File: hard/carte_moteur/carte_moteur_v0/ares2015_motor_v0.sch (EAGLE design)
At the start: 49 parts, among them IC1 ISO7220A, Q1 AOD417, U1 DRV8828PWP, U2 PCA9685

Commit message: schematic de la carte moteur finit !
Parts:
- removed A2, A3, A4: (no value), jumper:SJ
- removed HEADER: (no value), con-lsta:FE06-1
- removed IC2: (no value), SparkFun-PowerIC:V_REG_LM1117SOT223
- removed INPUT: MMATCH-6-, jt-con-micromatch:MMATCH-6-
- removed TP1, TP2, TP3: (no value), microbuilder:TESTPOINTROUND2MM
- removed U1: DRV8828PWP, Texas Instruments_By_element14_Batch_1:DRV8828PWP
- added 3V3LDO: (no value), SparkFun-PowerIC:V_REG_LM1117SOT223
- added C10, C15, C18: 0.47uF, adafruit:C-USC0805K
- added C12, C16, C6: 0.01uF, adafruit:C-USC0805K
- added C13, C17, C9: 0.1uF, adafruit:C-USC0805K
- added LED3, LED4, LED5: rouge, adafruit:LEDCHIPLED_0805
- added MOTOR0, MOTOR1, MOTOR2, MOTOR3: DRV8828PWP, Texas Instruments_By_element14_Batch_1:DRV8828PWP
- added OUT_MOT0, OUT_MOT2, OUT_MOT3: SL-3.5-2-90G, WEIDMULLER:SL-3.5-2-90G
- added PWM_ACCES, PWM_ACCES1: MMATCH-6-, jt-con-micromatch:MMATCH-6-
- added R15, R7: 0.25, adafruit:R-US_R0805
- added R8: 330, adafruit:R-US_R0805
- added U$6: LMD128D818, ADS128D818:LMD128D818
- R3, R6: value 10k -> 330
- R5: value 10k -> 0.25
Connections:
- net VIN renamed VIN_ARDUINO
- removed net C_DIR1: HEADER.4, INPUT.5
- removed net C_DIR2: HEADER.2, INPUT.7
- removed net C_PWM1: HEADER.3, INPUT.6
- removed net C_PWM2: HEADER.1, INPUT.8
- new net ADC0: MOTOR0.ISEN, MOTOR0.ISEN_2, R10.1, U$6.IN0
- new net ADC1: MOTOR1.ISEN, MOTOR1.ISEN_2, R5.1, U$6.IN1
- new net ADC2: MOTOR2.ISEN, MOTOR2.ISEN_2, R7.1, U$6.IN2
- new net ADC3: MOTOR3.ISEN, MOTOR3.ISEN_2, R15.1, U$6.IN3
- new net ADC4: U$6.IN4
- new net ADC5: U$6.IN5
- new net ADC6: U$6.IN6
- new net ADC7: U$6.IN7
- new net N$16: MOTOR0.OUT1, MOTOR0.OUT1_2, OUT_MOT0.1
- new net N$33: MOTOR1.OUT1, MOTOR1.OUT1_2, OUT_MOT1.1
- new net N$38: C12.1, MOTOR2.CP1
- new net N$40: C12.2, MOTOR2.CP2
- new net N$41: C13.1, MOTOR2.VCP
- new net N$42: LED4.C, MOTOR2.NFAULT
- new net N$43: LED4.A, R6.2
- new net N$46: MOTOR2.OUT1, MOTOR2.OUT1_2, OUT_MOT2.1
- new net N$47: MOTOR2.OUT2, MOTOR2.OUT2_2, OUT_MOT2.2
- new net N$48: C16.1, MOTOR3.CP1
- new net N$50: C17.1, MOTOR3.VCP
- new net N$51: LED5.C, MOTOR3.NFAULT
- new net N$52: LED5.A, R8.2
- new net N$53: MOTOR3.OUT1, MOTOR3.OUT1_2, OUT_MOT3.1
- new net N$54: MOTOR3.OUT2, MOTOR3.OUT2_2, OUT_MOT3.2
- new net N$7: MOTOR0.OUT2, MOTOR0.OUT2_2, OUT_MOT0.2
- new net V3POUT0: C1.1, MOTOR0.V3P3OUT, MOTOR0.VREF, MOTOR0.VREF_2
- new net V3POUT2: C15.1, MOTOR2.V3P3OUT, MOTOR2.VREF, MOTOR2.VREF_2
- new net V3POUT3: C18.1, MOTOR3.V3P3OUT, MOTOR3.VREF, MOTOR3.VREF_2
- net +12V: now also 3V3LDO.IN, C13.2, C17.2, C9.2, MOTOR0.VM, MOTOR0.VM_2, MOTOR1.VM, MOTOR1.VM_2, MOTOR2.VM, MOTOR2.VM_2, MOTOR3.VM, MOTOR3.VM_2; no longer IC2.IN, U1.VM, U1.VM_2
- net A0: now also U$6.A0
- net A1: now also U$6.A1
- net A2: no longer A2.2, R3.2, TP3.P$1
- net A3: no longer A3.1, R5.2, TP2.P$1
- net A4: no longer A4.1, R6.2, TP1.P$1
- net GND: now also 3V3LDO.ADJ, C10.2, C15.2, C18.2, MOTOR0.EPAD, MOTOR0.GND, MOTOR0.GND_2, MOTOR1.EPAD, MOTOR1.GND, MOTOR1.GND_2, MOTOR2.EPAD, MOTOR2.GND, MOTOR2.GND_2, MOTOR3.EPAD, MOTOR3.GND, MOTOR3.GND_2, PWM_ACCES.4, PWM_ACCES1.4, R15.2, R5.2, R7.2, U$6.GND; no longer HEADER.5, IC2.ADJ, INPUT.4, R3.1, R5.1, R6.1, U1.EPAD, U1.GND, U1.GND_2
- net N$12: now also C6.2, MOTOR1.CP2; no longer OUT_MOT1.2, U1.OUT2, U1.OUT2_2
- net N$14: now also C9.1, MOTOR1.VCP; no longer OUT_MOT1.1, U1.OUT1, U1.OUT1_2
- net N$18: now also LED3.C, MOTOR1.NFAULT; no longer IC1.INA, R13.1
- net N$19: now also LED3.A, R3.2; no longer IC1.INB, R14.1
- net N$35: now also MOTOR1.OUT2, MOTOR1.OUT2_2, OUT_MOT1.2; no longer R10.1, U1.ISEN, U1.ISEN_2
- net N$36: now also MOTOR0.CP1; no longer U1.CP1
- net N$37: now also MOTOR0.CP2; no longer U1.CP2
- net N$39: now also MOTOR0.VCP; no longer U1.VCP
- net N$45: now also MOTOR0.NFAULT; no longer U1.NFAULT
- net N$49: now also C16.2, MOTOR3.CP2; no longer U1.APHASE
- net N$6: now also C6.1, MOTOR1.CP1; no longer U1.ENBL
- net PWM0: now also MOTOR0.ENBL, PWM_ACCES.6
- net PWM1: now also MOTOR0.APHASE, PWM_ACCES.5
- net PWM2: now also MOTOR1.ENBL, PWM_ACCES.8
- net PWM3: now also MOTOR1.APHASE, PWM_ACCES.7
- net PWM4: now also MOTOR2.ENBL, PWM_ACCES1.6
- net PWM5: now also MOTOR2.APHASE, PWM_ACCES1.5
- net PWM6: now also MOTOR3.ENBL, PWM_ACCES1.8
- net PWM7: now also MOTOR3.APHASE, PWM_ACCES1.7
- net SCL: now also IC1.INB, R14.1, U$6.SCL
- net SDA: now also IC1.INA, R13.1, U$6.SDA
- net V3POUT1: now also C10.1, MOTOR1.V3P3OUT, MOTOR1.VREF, MOTOR1.VREF_2; no longer C1.1, U1.V3P3OUT, U1.VREF, U1.VREF_2
- net VCC: now also 3V3LDO.OUT, 3V3LDO.OUT@1, MOTOR0.DECAY, MOTOR0.I0, MOTOR0.I1, MOTOR0.I2, MOTOR0.I3, MOTOR0.I4, MOTOR0.NRESET, MOTOR0.NSLEEP, MOTOR1.DECAY, MOTOR1.I0, MOTOR1.I1, MOTOR1.I2, MOTOR1.I3, MOTOR1.I4, MOTOR1.NRESET, MOTOR1.NSLEEP, MOTOR2.DECAY, MOTOR2.I0, MOTOR2.I1, MOTOR2.I2, MOTOR2.I3, MOTOR2.I4, MOTOR2.NRESET, MOTOR2.NSLEEP, MOTOR3.DECAY, MOTOR3.I0, MOTOR3.I1, MOTOR3.I2, MOTOR3.I3, MOTOR3.I4, MOTOR3.NRESET, MOTOR3.NSLEEP, PWM_ACCES.3, PWM_ACCES1.3, R13.2, R14.2, R3.1, R6.1, R8.1, U$6.V+; no longer A2.1, A3.2, A4.2, HEADER.6, IC2.OUT, IC2.OUT@1, INPUT.3, U1.DECAY, U1.I0, U1.I1, U1.I2, U1.I3, U1.I4, U1.NRESET, U1.NSLEEP
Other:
- note added: "Générateur PWM"
- note added: "I2C -> PWM generation -> ADC -> galvanic isolation"
- note added: "ISO1541 (isolateur bus I2C)"
- note added: "Les switch permettent de relier le GND_CLEAN au GND et 12V à VIN (et d'eviter l'utilisation de la carte alim)"
- note added: "MANQUE UN CONNECTEUR POUR l'I2C"
- note added: "MOS pour la protection de l'inversion de polarité"
- note added: "Permet de choisir par des soudure 2 bits sur l'identifiant de l'I2C"
- note added: "Power Managment"
- note added: "Théo S. pour Ares"
- note added: "Utile ?"
- moved on the sheet: A0, A1, C1, C11, C14, C2, C3, C4, C5, C7, C8, IC1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

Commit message: modifs mineures
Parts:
- removed U$2, U$3, U$4: FIDUCIAL, adafruit:FIDUCIAL
- 3V3LDO: MF (none) -> NXP; MPN (none) -> ACT108W-600D; OC_FARNELL (none) -> 2074968
- A0, A1, C4, C5, LED1, LED2, LED3, LED4, LED5, MOTOR0, MOTOR1, MOTOR2, MOTOR3, PWM_ACCES, PWM_ACCES1, PWR, PWR1, Q1, TP4, TP5, U$1, U$5, U$6, U2: OC_FARNELL (none) -> unknown
- C1, C10, C15, C18: MF (none) -> AVX; MPN (none) -> 04026D474KAT2A; OC_FARNELL (none) -> 1740587
- C11, C13, C14, C17, C2, C3, C8, C9: MF (none) -> AVX; MPN (none) -> 02016D104KAT2A; OC_FARNELL (none) -> 1657913
- C12, C16, C6, C7: MF (none) -> AVX; MPN (none) -> 0201ZC103KAT2A; OC_FARNELL (none) -> 2280757
- IC1: value ISO7220A -> ISO1541; MF (none) -> TEXAS INSTRUMENTS
- IN_MOT1, OUT_MOT0, OUT_MOT1, OUT_MOT2, OUT_MOT3: MF (none) -> WEIDMULLER; MPN (none) -> SL 3.5/2/90G; OC_FARNELL (none) -> 1121786
- R1, R10, R12, R13, R14, R15, R2, R3, R4, R5, R6, R7, R8, R9: device adafruit:R-US_R0805 -> adafruit:R-US_M0805; OC_FARNELL (none) -> unknown
- R11: value 135k -> 1.5k; device adafruit:R-US_R0805 -> adafruit:R-US_M0805; OC_FARNELL (none) -> unknown
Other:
- moved on the sheet: R13

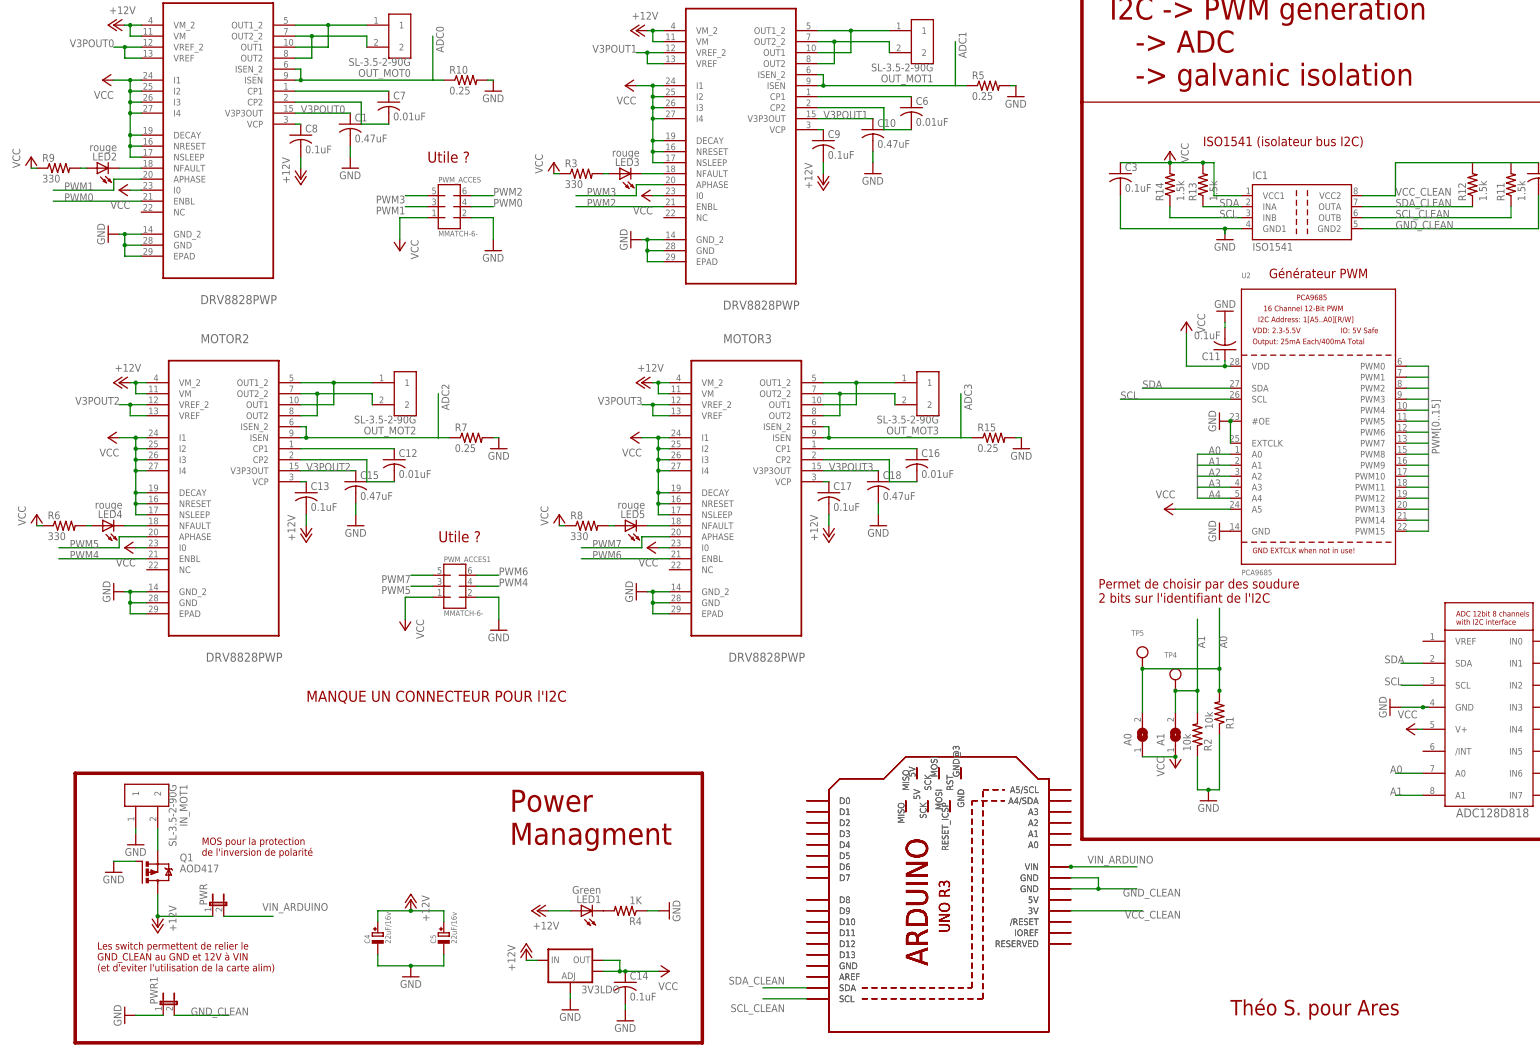
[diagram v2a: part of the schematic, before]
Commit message: routage : automatique=98,8% réussite. Reste à ajouter les deux autres hacheurs
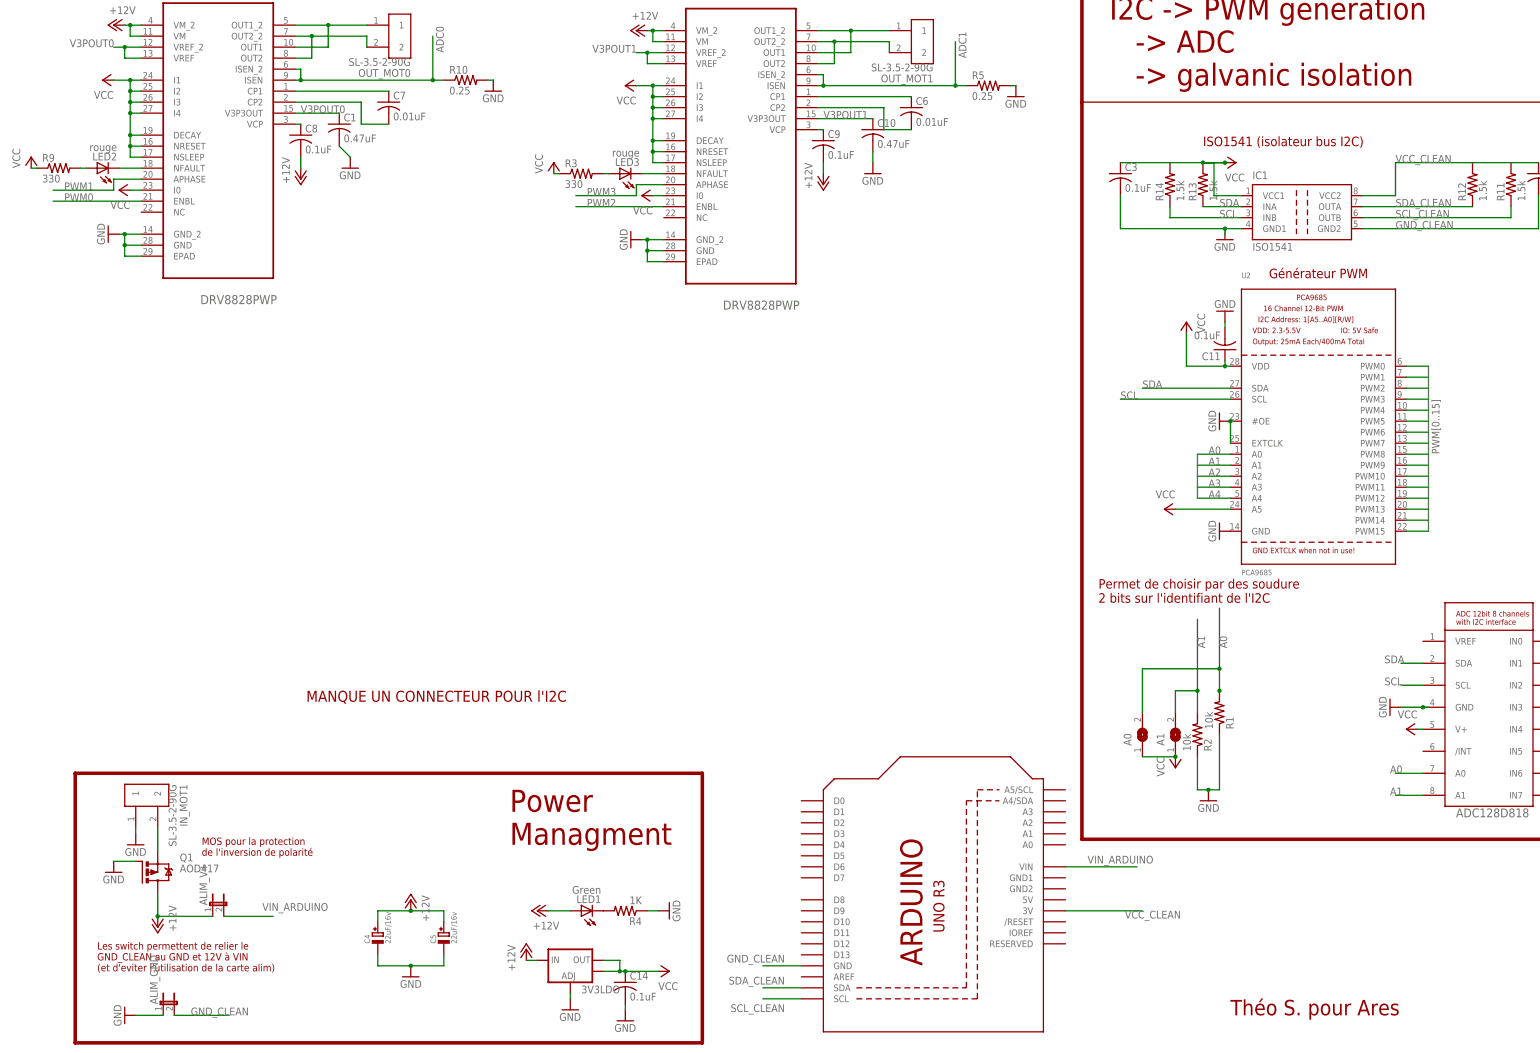
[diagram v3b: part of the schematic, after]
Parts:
- removed C12, C16: 0.01uF, adafruit:C-USC0805K
- removed C13, C17: 0.1uF, adafruit:C-USC0805K
- removed C15, C18: 0.47uF, adafruit:C-USC0805K
- removed LED4, LED5: rouge, adafruit:LEDCHIPLED_0805
- removed MOTOR2, MOTOR3: DRV8828PWP, Texas Instruments_By_element14_Batch_1:DRV8828PWP
- removed OUT_MOT2, OUT_MOT3: SL-3.5-2-90G, WEIDMULLER:SL-3.5-2-90G
- removed PWM_ACCES, PWM_ACCES1: MMATCH-6-, jt-con-micromatch:MMATCH-6-
- removed R15, R7: 0.25, adafruit:R-US_M0805
- removed R6, R8: 330, adafruit:R-US_M0805
- removed TP4, TP5: (no value), microbuilder:TESTPOINTROUND2MM
- removed U$1, U$5: ARDUINO_R3_ICSP, adafruit:ARDUINO_R3_ICSP
- added U1: ARDUINOR3-BPLACE, adafruit:ARDUINOR3-BPLACE
- renumbered PWR to ALIM_V+, PWR1 to ALIM_GND
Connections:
- removed net N$10: U$1.GND@3, U$5.GND@3
- removed net N$11: U$1.SCK, U$5.SCK
- removed net N$13: U$1.RST, U$5.RST
- removed net N$3: U$1.MISO, U$5.MISO
- removed net N$34: U$1.GND, U$5.GND
- removed net N$38: C12.1, MOTOR2.CP1
- removed net N$40: C12.2, MOTOR2.CP2
- removed net N$41: C13.1, MOTOR2.VCP
- removed net N$42: LED4.C, MOTOR2.NFAULT
- removed net N$43: LED4.A, R6.2
- removed net N$46: MOTOR2.OUT1, MOTOR2.OUT1_2, OUT_MOT2.1
- removed net N$47: MOTOR2.OUT2, MOTOR2.OUT2_2, OUT_MOT2.2
- removed net N$48: C16.1, MOTOR3.CP1
- removed net N$49: C16.2, MOTOR3.CP2
- removed net N$5: U$1.5V@1, U$5.5V@1
- removed net N$50: C17.1, MOTOR3.VCP
- removed net N$51: LED5.C, MOTOR3.NFAULT
- removed net N$52: LED5.A, R8.2
- removed net N$53: MOTOR3.OUT1, MOTOR3.OUT1_2, OUT_MOT3.1
- removed net N$54: MOTOR3.OUT2, MOTOR3.OUT2_2, OUT_MOT3.2
- removed net N$8: U$1.MOSI, U$5.MOSI
- removed net V3POUT2: C15.1, MOTOR2.V3P3OUT, MOTOR2.VREF, MOTOR2.VREF_2
- removed net V3POUT3: C18.1, MOTOR3.V3P3OUT, MOTOR3.VREF, MOTOR3.VREF_2
- net +12V: no longer C13.2, C17.2, MOTOR2.VM, MOTOR2.VM_2, MOTOR3.VM, MOTOR3.VM_2
- net /RST: now also U1./RESET; no longer U$1./RESET, U$5./RESET
- net A0: no longer TP5.P$1
- net A1: no longer TP4.P$1
- net ADC2: no longer MOTOR2.ISEN, MOTOR2.ISEN_2, R7.1
- net ADC3: no longer MOTOR3.ISEN, MOTOR3.ISEN_2, R15.1
- net GND: no longer C15.2, C18.2, MOTOR2.EPAD, MOTOR2.GND, MOTOR2.GND_2, MOTOR3.EPAD, MOTOR3.GND, MOTOR3.GND_2, PWM_ACCES.4, PWM_ACCES1.4, R15.2, R7.2
- net GND_CLEAN: now also U1.GND; no longer U$1.GND@1, U$1.GND@2, U$5.GND@1, U$5.GND@2
- net N$1: now also U1.IOREF; no longer U$1.IOREF, U$5.IOREF
- net N$15: now also U1.A5/SCL; no longer U$1.A5/SCL, U$5.A5/SCL
- net N$17: now also U1.A4/SDA; no longer U$1.A4/SDA, U$5.A4/SDA
- net N$2: now also U1.RESERVED; no longer U$1.RESERVED, U$5.RESERVED
- net N$20: now also U1.A0; no longer U$1.A0, U$5.A0
- net N$21: now also U1.A1; no longer U$1.A1, U$5.A1
- net N$22: now also U1.A2; no longer U$1.A2, U$5.A2
- net N$23: now also U1.A3; no longer U$1.A3, U$5.A3
- net N$24: now also U1.D0; no longer U$1.D0, U$5.D0
- net N$25: now also U1.D1; no longer U$1.D1, U$5.D1
- net N$26: now also U1.D2; no longer U$1.D2, U$5.D2
- net N$27: now also U1.D4; no longer U$1.D4, U$5.D4
- net N$28: now also U1.D7; no longer U$1.D7, U$5.D7
- net N$29: now also U1.D8; no longer U$1.D8, U$5.D8
- net N$30: now also U1.D12; no longer U$1.D12, U$5.D12
- net N$31: now also U1.D13; no longer U$1.D13, U$5.D13
- net N$32: now also U1.AREF; no longer U$1.AREF, U$5.AREF
- net N$4: now also U1.D9; no longer U$1.D9, U$5.D9
- net N$9: now also U1.5V; no longer U$1.5V, U$5.5V
- net PWM0: no longer PWM_ACCES.6
- net PWM0A: now also U1.D6; no longer U$1.D6, U$5.D6
- net PWM0B: now also U1.D5; no longer U$1.D5, U$5.D5
- net PWM1: no longer PWM_ACCES.5
- net PWM1B: now also U1.D10; no longer U$1.D10, U$5.D10
- net PWM2: no longer PWM_ACCES.8
- net PWM2A: now also U1.D11; no longer U$1.D11, U$5.D11
- net PWM2B: now also U1.D3; no longer U$1.D3, U$5.D3
- net PWM3: no longer PWM_ACCES.7
- net PWM4: no longer MOTOR2.ENBL, PWM_ACCES1.6
- net PWM5: no longer MOTOR2.APHASE, PWM_ACCES1.5
- net PWM6: no longer MOTOR3.ENBL, PWM_ACCES1.8
- net PWM7: no longer MOTOR3.APHASE, PWM_ACCES1.7
- net SCL_CLEAN: now also U1.SCL; no longer U$1.SCL, U$5.SCL
- net SDA_CLEAN: now also U1.SDA; no longer U$1.SDA, U$5.SDA
- net VCC: no longer MOTOR2.DECAY, MOTOR2.I0, MOTOR2.I1, MOTOR2.I2, MOTOR2.I3, MOTOR2.I4, MOTOR2.NRESET, MOTOR2.NSLEEP, MOTOR3.DECAY, MOTOR3.I0, MOTOR3.I1, MOTOR3.I2, MOTOR3.I3, MOTOR3.I4, MOTOR3.NRESET, MOTOR3.NSLEEP, PWM_ACCES.3, PWM_ACCES1.3, R6.1, R8.1
- net VCC_CLEAN: now also U1.3V; no longer U$1.3V, U$5.3V
- net VIN_ARDUINO: now also U1.VIN; no longer U$1.VIN, U$5.VIN
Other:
- note removed: "Utile ?"
- moved on the sheet: C1
